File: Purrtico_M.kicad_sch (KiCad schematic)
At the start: 122 parts, among them J1 Conn_02x05_Odd_Even, J2 Conn_01x02, J4 Conn_01x02, U1 OPA1679, U2 OPA1679, U3 OPA1679

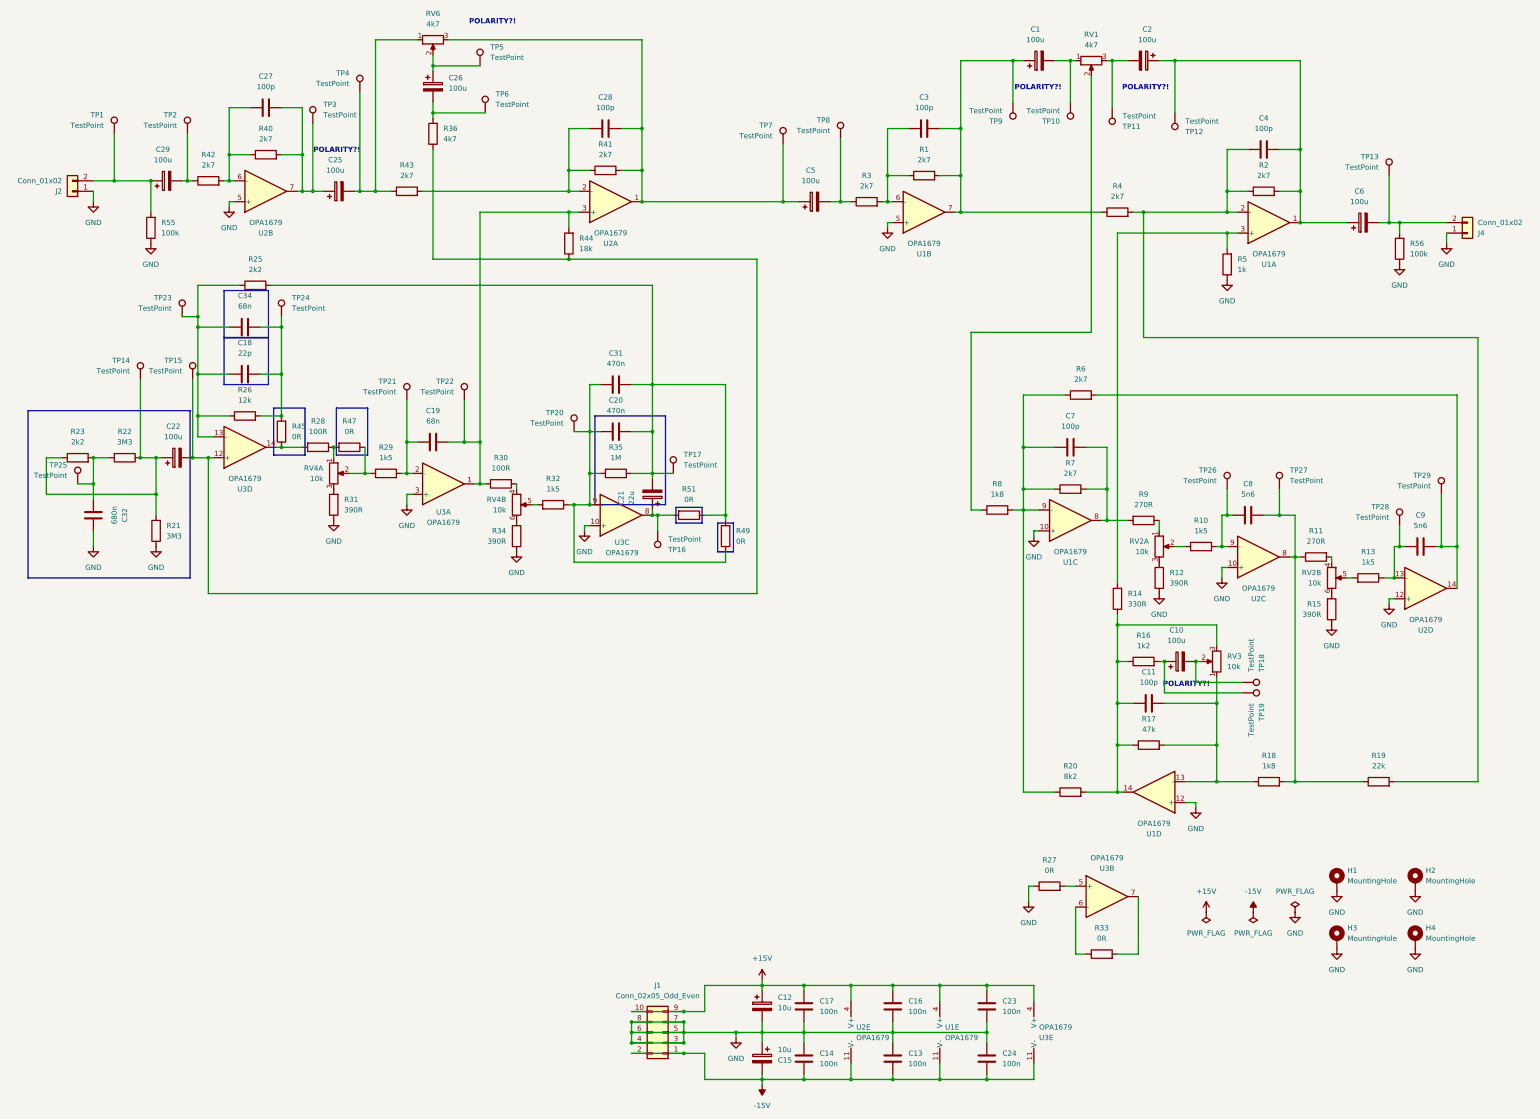
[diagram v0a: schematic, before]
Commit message: first update after testing
shelving circuit not working for whatever reason :/
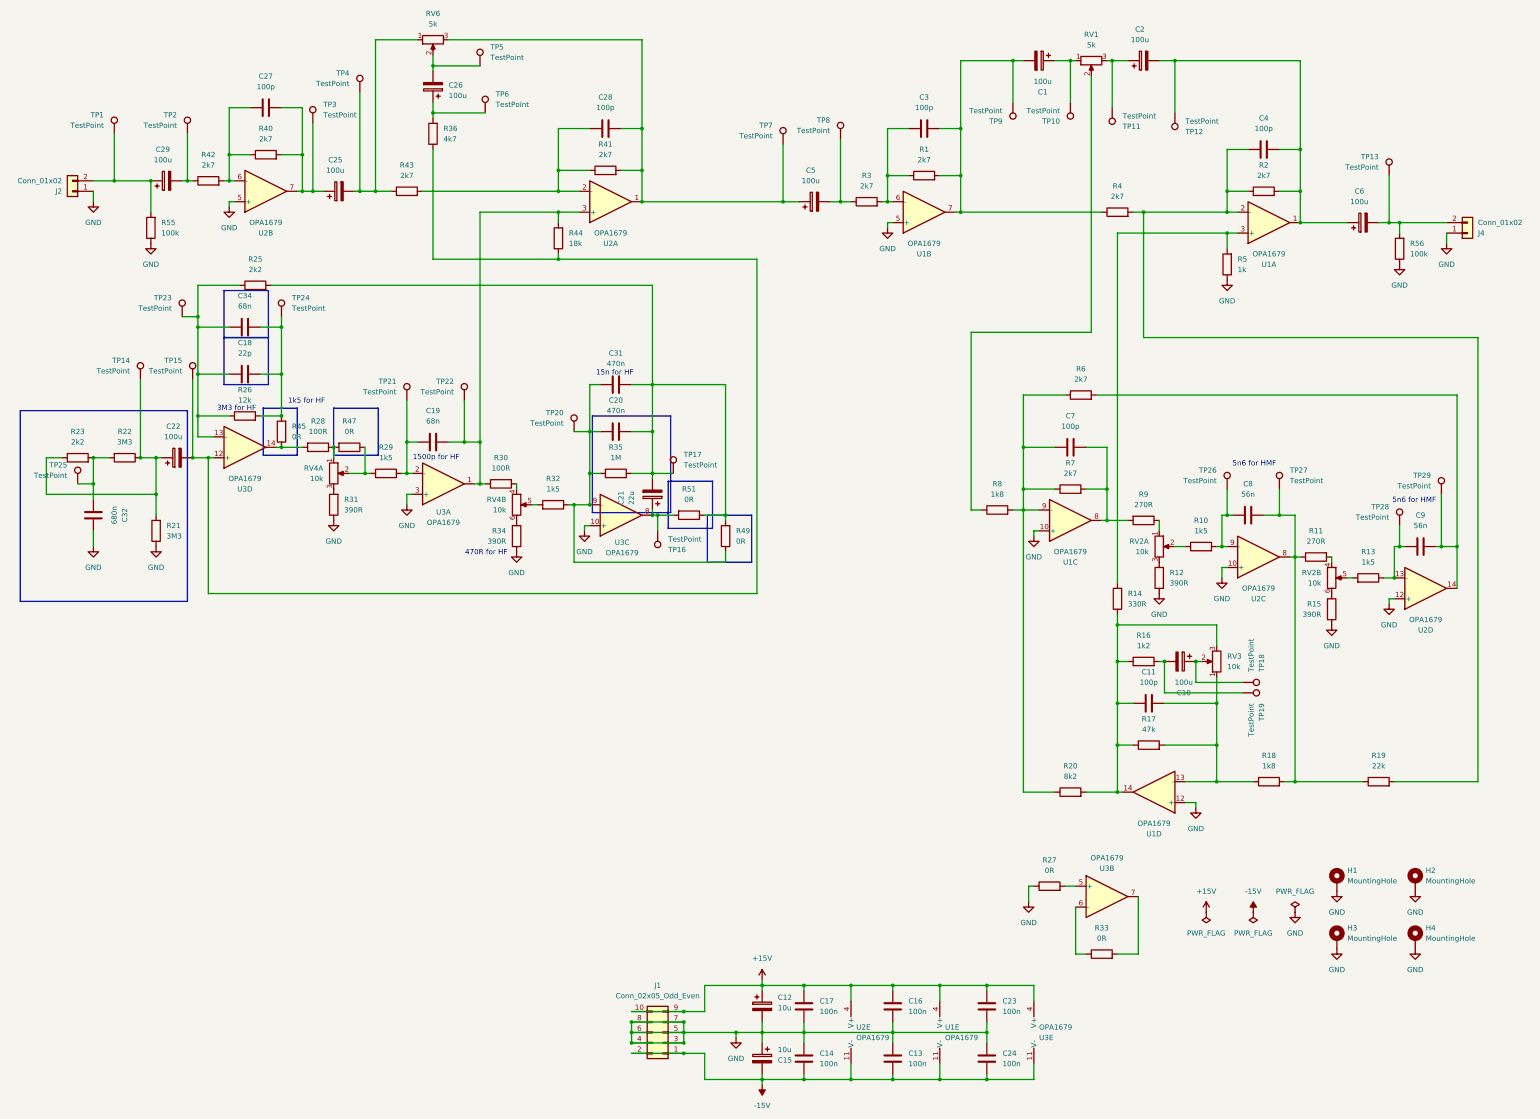
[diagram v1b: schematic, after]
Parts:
- C8, C9: value 5n6 -> 56n
- RV1, RV6: value 4k7 -> 5k
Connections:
- net at RV6.2, TP5.1: now also C26.2; no longer C26.1
- net at R36.2, TP6.1: now also C26.1; no longer C26.2
- net at RV1.1, TP10.1: now also C1.1; no longer C1.2
- net at RV1.3, TP11.1: now also C2.1; no longer C2.2
- net at C4.2, C6.1, R2.2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: now also C2.2; no longer C2.1
- net at C3.2, R1.2, R4.1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: now also C1.2; no longer C1.1
- net at R16.2, TP19.1: now also C10.2; no longer C10.1
- net at RV3.2, TP18.1: now also C10.1; no longer C10.2
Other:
- note added: "1500p for HF"
- note added: "15n for HF"
- note added: "1k5 for HF"
- note added: "3M3 for HF"
- note added: "470R for HF"
- note added: "5n6 for HMF"
- note removed: "POLARITY?!"
- moved on the sheet: C1, C10, C2, C26, R44

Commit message: update schematic
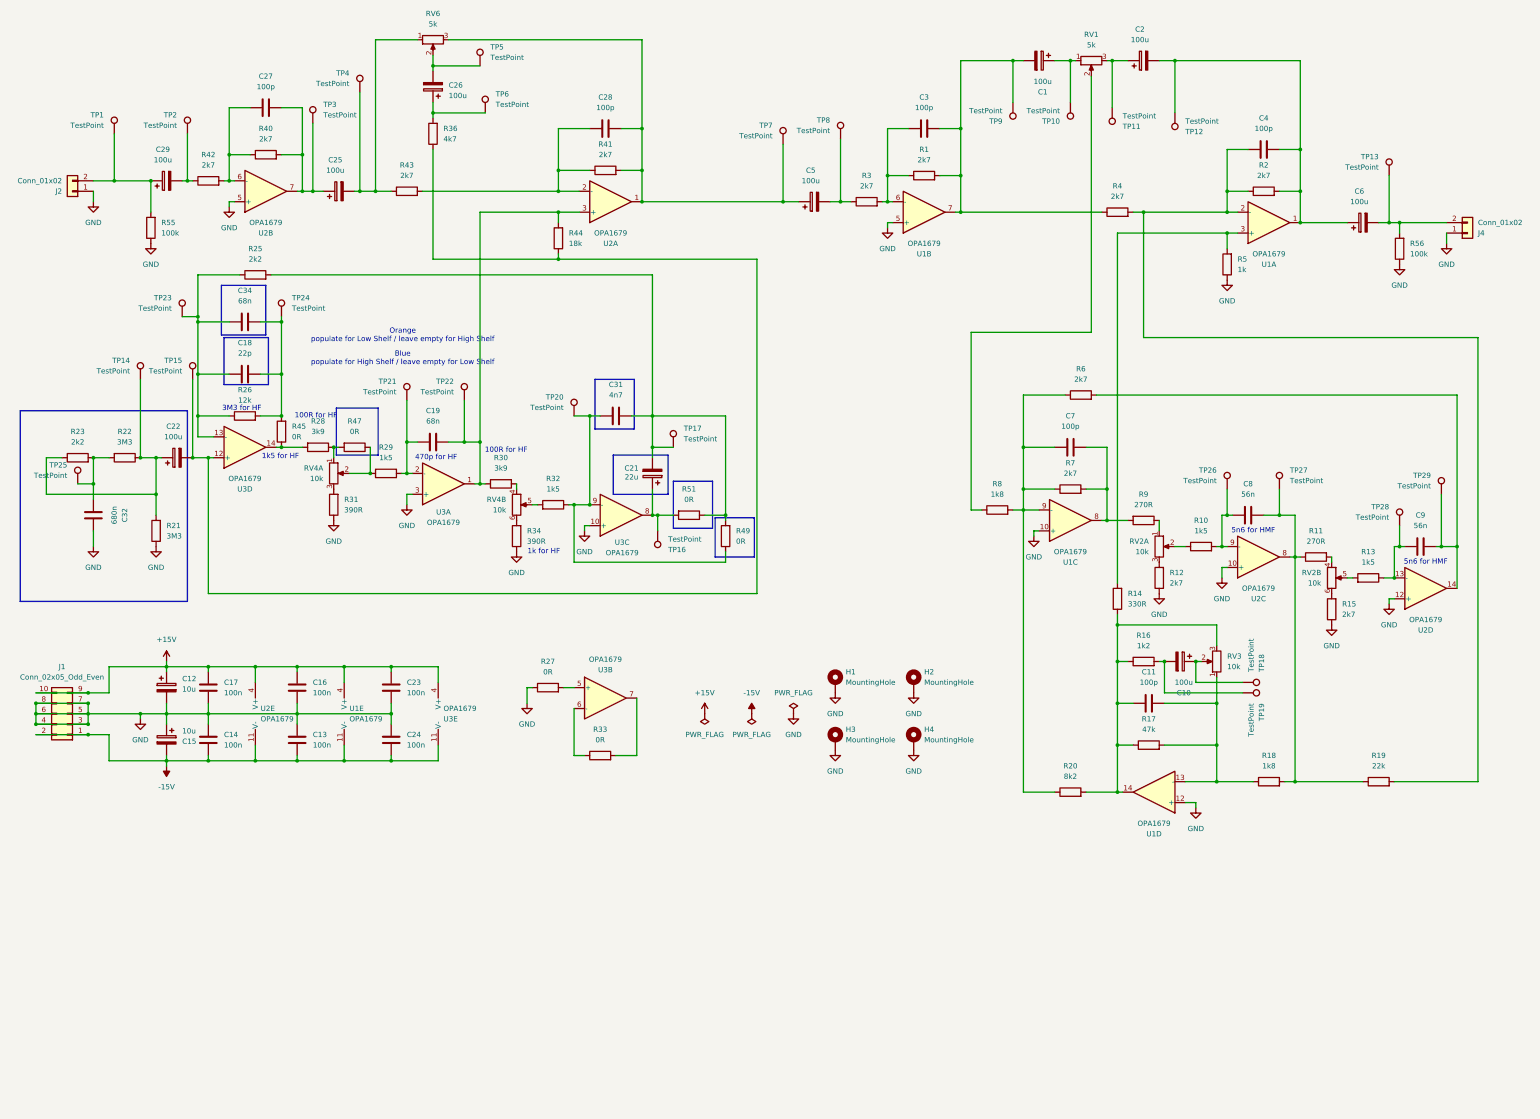
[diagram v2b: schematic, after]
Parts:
- removed C20: 470n, Capacitor_THT:C_Rect_L7.2mm_W2.5mm_P5.00mm_FKS2_FKP2_MKS2_MKP2, symbol Device:C
- removed R35: 1M, Resistor_SMD:R_1206_3216Metric, symbol Device:R
- C31: value 470n -> 4n7
- R12, R15: value 390R -> 2k7
- R28, R30: value 100R -> 3k9
- TP1, TP10, TP11, TP12, TP13, TP14, TP15, TP17, TP18, TP19, TP2, TP20, TP21, TP22, TP23, TP24, TP26, TP27, TP28, TP29, TP3, TP4, TP5, TP6, TP7, TP8, TP9: now left out of the parts list
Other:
- note added: "100R for HF"
- note added: "1k for HF"
- note added: "470p for HF"
- note added: "Blue populate for High Shelf / leave empty for Low Shelf"
- note added: "Orange populate for Low Shelf / leave empty for High Shelf"
- note removed: "1500p for HF"
- note removed: "15n for HF"
- note removed: "470R for HF"
- moved on the sheet: C12, C13, C14, C15, C16, C17, C21, C23, C24, C31, C34, H1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

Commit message: update pcb
added 470p cap as MLCC, removed two mounting holes to create space for wider potentiometer spacing, swapped rows of RV6 to enable the use of a single gang potentiometer for the high shelf
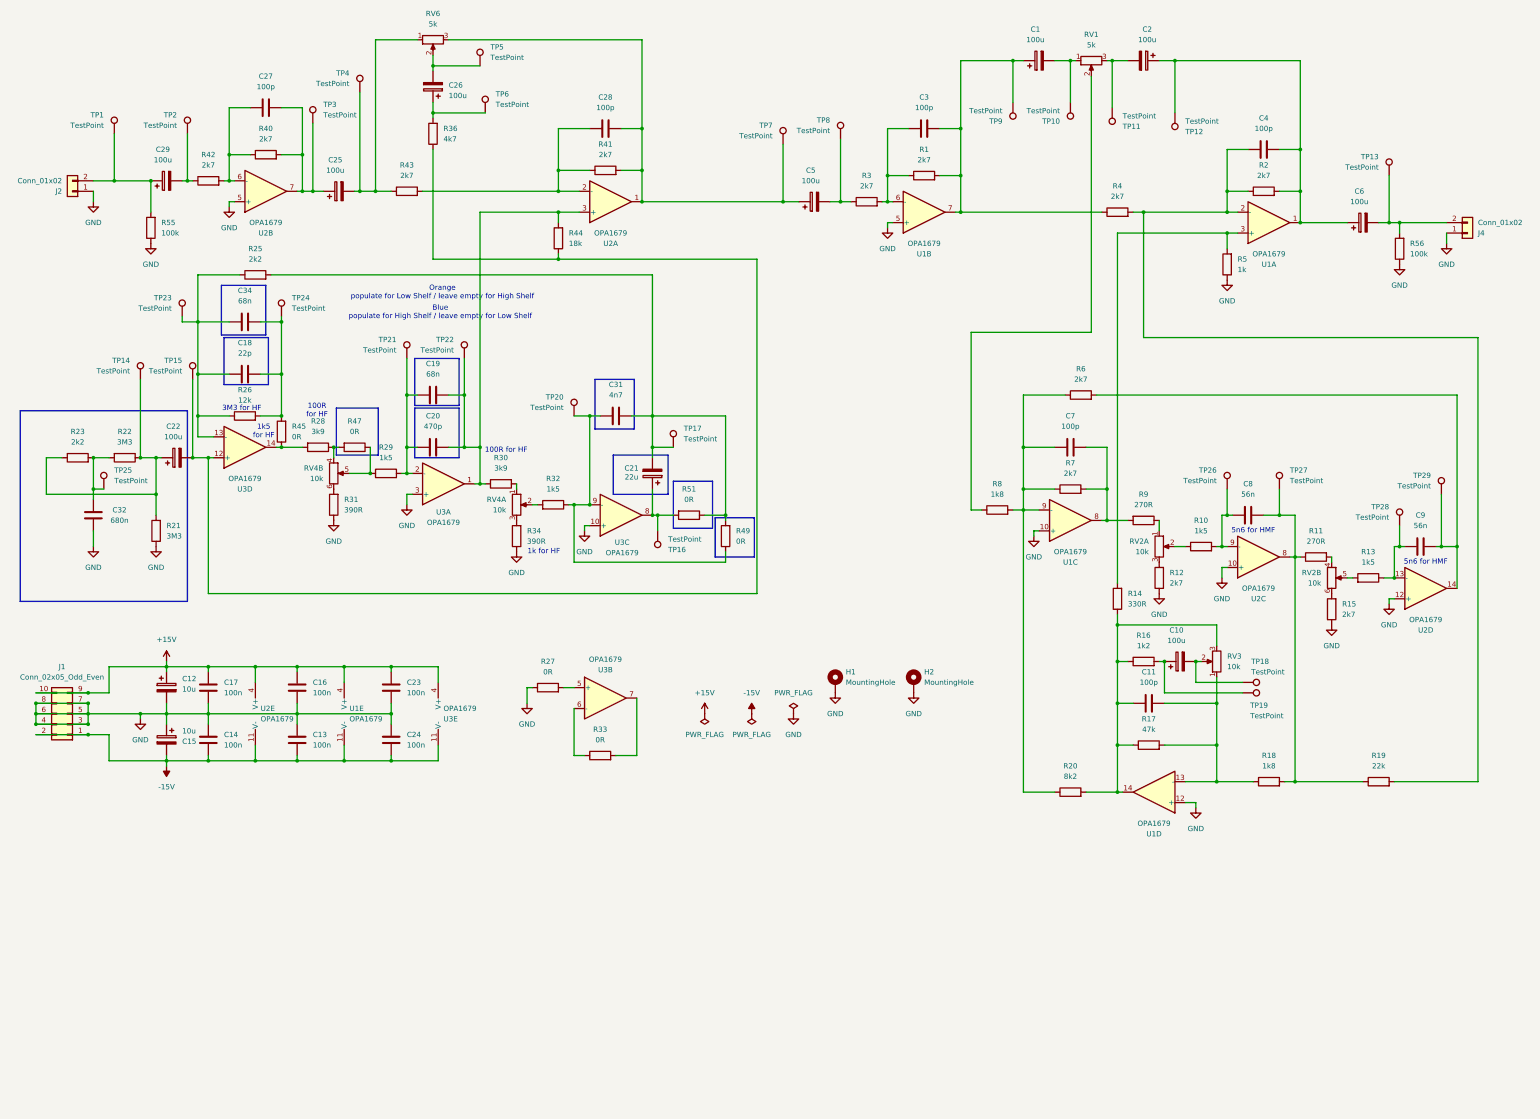
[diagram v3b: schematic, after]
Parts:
- removed H3, H4: MountingHole, MountingHole:MountingHole_3.2mm_M3_DIN965_Pad, symbol Mechanical:MountingHole_Pad
- added C20: 470p, Capacitor_SMD:C_1206_3216Metric, symbol Device:C
- TP16, TP25: now left out of the parts list
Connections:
- net at C19.1, R29.2, TP21.1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: now also C20.1
- net at RV1.1, TP10.1: now also C1.2; no longer C1.1
- net at RV1.3, TP11.1: now also C2.2; no longer C2.1
- net at C19.2, R30.1, R44.2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: now also C20.2
- net at C4.2, C6.1, R2.2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: now also C2.1; no longer C2.2
- net at C3.2, R1.2, R4.1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: now also C1.1; no longer C1.2
- net at R16.2, TP19.1: now also C10.1; no longer C10.2
- net at RV3.2, TP18.1: now also C10.2; no longer C10.1
- net at R28.1, R47.2: now also RV4.4; no longer RV4.1
- net at R30.2: now also RV4.1; no longer RV4.4
- net at RV4.5: now also R29.1, R47.1; no longer R32.2
- net at RV4.6: now also R31.2; no longer R34.2
- net at RV4.3: now also R34.2; no longer R31.2
- new net: R32.2, RV4.2
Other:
- note removed: "470p for HF"
- moved on the sheet: C1, C10, C19, C2, RV4A, RV4B, TP21, TP22, TP25
